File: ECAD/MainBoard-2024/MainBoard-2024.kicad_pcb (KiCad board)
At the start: 2 copper layers, 100 x 100 mm, 64 parts, among them J1 XT60, J10 Conn_01x02, J11 Conn_01x03, J12 Conn_01x04, J13 Conn_01x03, J14 Conn_01x03, J16 XT30, J17 XT30, J18 Tirette, J2 Conn_01x04, J20 BAU, J21 BAU, J22 Conn_01x04, J23 Conn_01x02, J26 BAU, J27 BAU, J28 Conn_01x02, J29 Conn_01x02, J3 ConStep1, J30 Conn_01x03, J4 Conn_01x02, J5 ConStep1, J6 ConStep1, J7 XT30, J8 Conn_01x02, J9 Conn_01x02, K2 FINDER-36.11, U1 Teensy3.5_All_Pins, U2 R-78B3.3-2.0, U3 R-78B12-2.0, U4 R-78B5.0-2.0

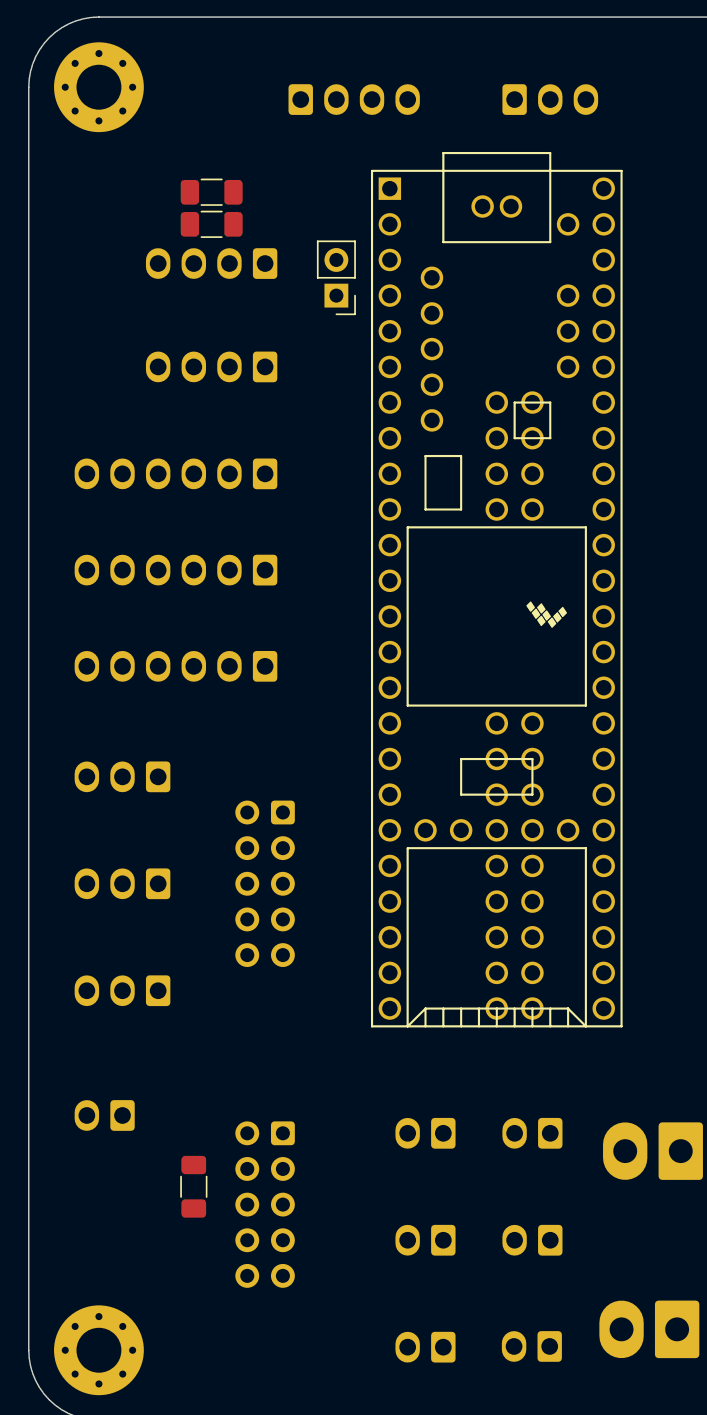
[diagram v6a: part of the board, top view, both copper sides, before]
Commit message: Multiple updates
- Change connectors positions
- Change Teensy position (for the USB port)
- Add connector for init button
- Add 5V signal on the Ihm connecto
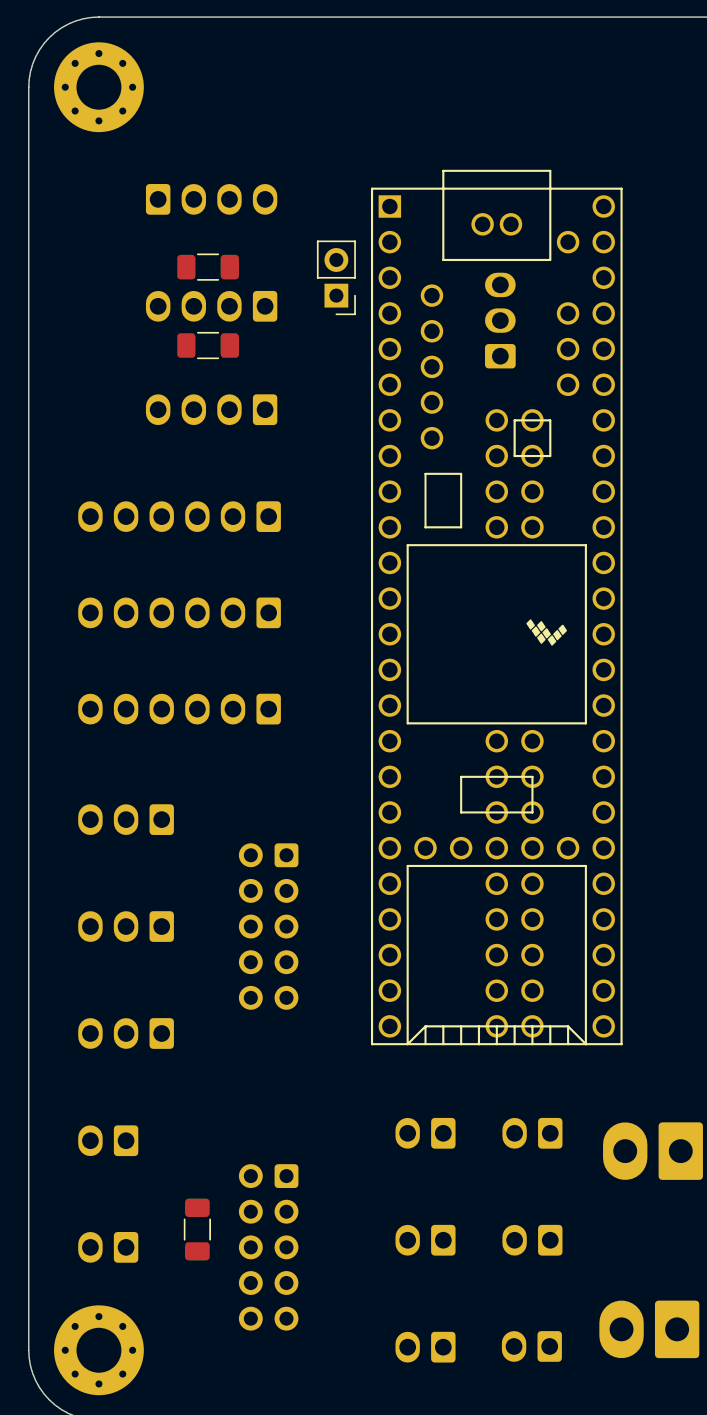
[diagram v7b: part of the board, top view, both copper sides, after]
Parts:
- added J15: Conn_01x02, Connector_Molex:Molex_KK-254_AE-6410-02A_1x02_P2.54mm_Vertical, B.Cu at (106.9, 137.7)
- J18: value Tirette -> Conn_01x02
- moved J30 18.3 mm to (133.6, 74.2), turned to 90 degrees
- moved J12 12.4 mm to (109.2, 63.0)
- moved R22 8.64 mm to (112.8, 73.4)
- moved R21 5.34 mm to (112.8, 67.8)
- moved Con-TFT1 3.06 mm to (118.4, 132.6)
- moved J11 3.06 mm to (109.5, 114.8)
- moved J13 3.06 mm to (109.5, 107.2)
- moved J14 3.06 mm to (109.5, 122.4)
- moved J3 3.06 mm to (117.1, 92.5)
- moved J5 3.06 mm to (117.1, 85.6)
- moved R6 3.06 mm to (112.0, 136.4)
- moved IHM-IO1 3.06 mm to (118.4, 109.7)
- moved J6 3.06 mm to (117.1, 99.3)
- moved J22 3.05 mm to (116.8, 70.6)
- moved J2 3.05 mm to (116.8, 78.0)
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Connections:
- IHM-IO1 pad 2: Init -> +5V
- J12 pad 3: +5VP -> +5V
